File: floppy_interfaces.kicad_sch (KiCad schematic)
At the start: 24 parts, among them J13 Conn_01x04_Male, J14 Conn_02x17_Odd_Even, J16 Conn_01x04_Male, J6 SDF-60J for IEC 1541 serial p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, U1 74LS373, U2 74LVC374, U22 74LS06N, U3 74LVC374, U4 74LS373

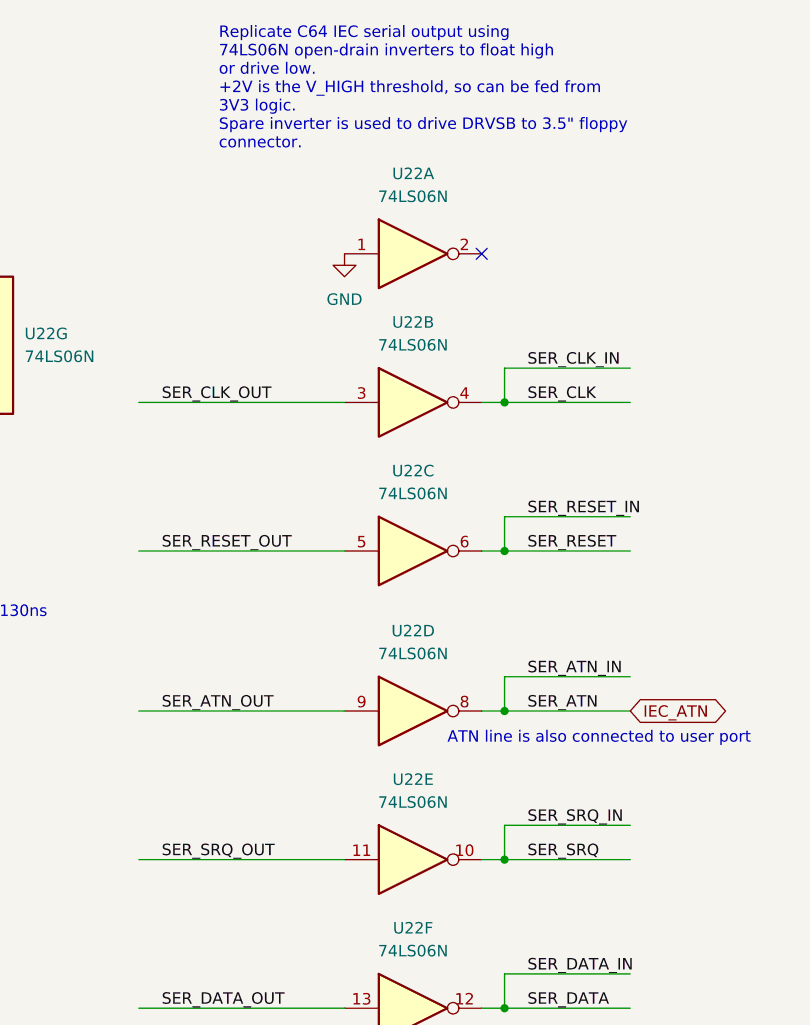
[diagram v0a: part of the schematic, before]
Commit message: route IEC port. Remove duplicate footprints
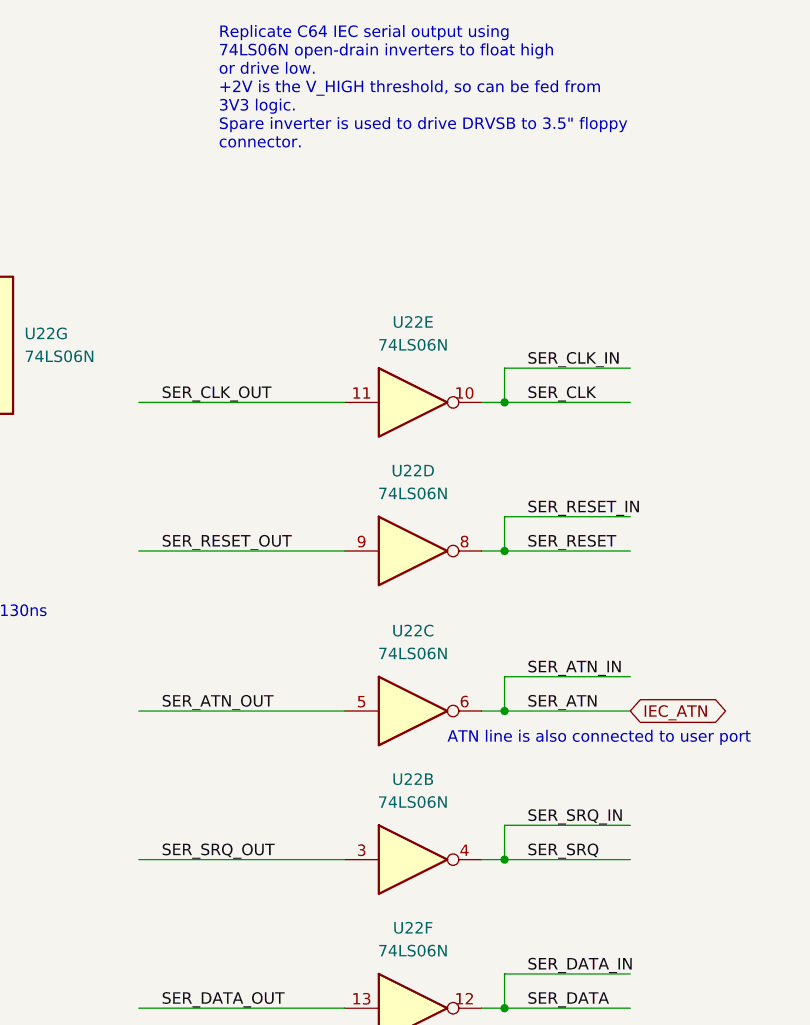
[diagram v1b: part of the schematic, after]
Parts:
- removed unit 1 of U22
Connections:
- net IEC_ATN: now also U22.6; no longer U22.8
- net SER_ATN_OUT: now also U22.5; no longer U22.9
- net SER_CLK: now also U22.10; no longer U22.4
- net SER_CLK_OUT: now also U22.11; no longer U22.3
- net SER_RESET: now also U22.8; no longer U22.6
- net SER_RESET_OUT: now also U22.9; no longer U22.5
- net SER_SRQ: now also U22.4; no longer U22.10
- net SER_SRQ_OUT: now also U22.3; no longer U22.11
- no-connect marks 19 -> 18
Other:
- moved on the sheet: U22B, U22C, U22D, U22E
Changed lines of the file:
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@@
   (no_connect (at 69.85 107.95))
   (no_connect (at 44.45 168.91))
-  (no_connect (at 165.1 45.72))
   (no_connect (at 69.85 168.91))
   (no_connect (at 69.85 171.45))
@@
     (pin "2")
   )
-  (symbol (lib_id "74xx:74LS06N") (at 157.48 45.72 0) (unit 1)
-    (in_bom yes) (on_board yes) (fields_autoplaced)
-    (property "Reference" "U22" (id 0) (at 157.48 36.83 0))
-    (property "Value" "74LS06N" (id 1) (at 157.48 39.37 0))
-    (property "Footprint" "Package_DIP:DIP-14_W7.62mm" (id 2) (at 157.48 45.72 0)
-      (effects (font (size 1.27 1.27)) hide)
-    )
-    (property "Datasheet" "http://www.ti.com/lit/gpn/sn74LS06N" (id 3) (at 157.48 45.72 0)
-      (effects (font (size 1.27 1.27)) hide)
-    )
-    (pin "1")
-    (pin "2")
-  )
   (symbol (lib_id "power:GND") (at 226.06 148.59 0) (unit 1)
     (in_bom yes) (on_board yes) (fields_autoplaced)
@@
     (pin "9")
   )
-  (symbol (lib_id "power:GND") (at 149.86 45.72 0) (unit 1)
-    (in_bom yes) (on_board yes) (fields_autoplaced)
-    (property "Reference" "#PWR0111" (id 0) (at 149.86 52.07 0)
-      (effects (font (size 1.27 1.27)) hide)
-    )
-    (property "Value" "GND" (id 1) (at 149.86 50.8 0))
-    (property "Footprint" "" (id 2) (at 149.86 45.72 0)
-      (effects (font (size 1.27 1.27)) hide)
-    )
-    (property "Datasheet" "" (id 3) (at 149.86 45.72 0)
-      (effects (font (size 1.27 1.27)) hide)
-    )
-    (pin "1")
-  )
   (symbol (lib_id "pspice:R") (at 38.1 97.79 90) (unit 1)
     (in_bom yes) (on_board yes)
@@
     (pin "1")
   )
-  (symbol (lib_id "74xx:74LS06N") (at 157.48 62.23 0) (unit 2)
-    (in_bom yes) (on_board yes) (fields_autoplaced)
-    (property "Reference" "U22" (id 0) (at 157.48 53.34 0))
-    (property "Value" "74LS06N" (id 1) (at 157.48 55.88 0))
-    (property "Footprint" "Package_DIP:DIP-14_W7.62mm" (id 2) (at 157.48 62.23 0)
-      (effects (font (size 1.27 1.27)) hide)
-    )
-    (property "Datasheet" "http://www.ti.com/lit/gpn/sn74LS06N" (id 3) (at 157.48 62.23 0)
+  (symbol (lib_id "74xx:74LS06N") (at 157.48 113.03 0) (unit 2)
+    (in_bom yes) (on_board yes) (fields_autoplaced)
+    (property "Reference" "U22" (id 0) (at 157.48 104.14 0))
+    (property "Value" "74LS06N" (id 1) (at 157.48 106.68 0))
+    (property "Footprint" "Package_DIP:DIP-14_W7.62mm" (id 2) (at 157.48 113.03 0)
+      (effects (font (size 1.27 1.27)) hide)
+    )
+    (property "Datasheet" "http://www.ti.com/lit/gpn/sn74LS06N" (id 3) (at 157.48 113.03 0)
       (effects (font (size 1.27 1.27)) hide)
     )
@@
     (pin "1")
   )
-  (symbol (lib_id "74xx:74LS06N") (at 157.48 78.74 0) (unit 3)
-    (in_bom yes) (on_board yes) (fields_autoplaced)
-    (property "Reference" "U22" (id 0) (at 157.48 69.85 0))
-    (property "Value" "74LS06N" (id 1) (at 157.48 72.39 0))
-    (property "Footprint" "Package_DIP:DIP-14_W7.62mm" (id 2) (at 157.48 78.74 0)
-      (effects (font (size 1.27 1.27)) hide)
-    )
-    (property "Datasheet" "http://www.ti.com/lit/gpn/sn74LS06N" (id 3) (at 157.48 78.74 0)
+  (symbol (lib_id "74xx:74LS06N") (at 157.48 96.52 0) (unit 3)
+    (in_bom yes) (on_board yes) (fields_autoplaced)
+    (property "Reference" "U22" (id 0) (at 157.48 87.63 0))
+    (property "Value" "74LS06N" (id 1) (at 157.48 90.17 0))
+    (property "Footprint" "Package_DIP:DIP-14_W7.62mm" (id 2) (at 157.48 96.52 0)
+      (effects (font (size 1.27 1.27)) hide)
+    )
+    (property "Datasheet" "http://www.ti.com/lit/gpn/sn74LS06N" (id 3) (at 157.48 96.52 0)
       (effects (font (size 1.27 1.27)) hide)
     )
@@
     (pin "6")
   )
-  (symbol (lib_id "74xx:74LS06N") (at 157.48 113.03 0) (unit 5)
-    (in_bom yes) (on_board yes) (fields_autoplaced)
-    (property "Reference" "U22" (id 0) (at 157.48 104.14 0))
-    (property "Value" "74LS06N" (id 1) (at 157.48 106.68 0))
-    (property "Footprint" "Package_DIP:DIP-14_W7.62mm" (id 2) (at 157.48 113.03 0)
-      (effects (font (size 1.27 1.27)) hide)
-    )
-    (property "Datasheet" "http://www.ti.com/lit/gpn/sn74LS06N" (id 3) (at 157.48 113.03 0)
+  (symbol (lib_id "74xx:74LS06N") (at 157.48 62.23 0) (unit 5)
+    (in_bom yes) (on_board yes) (fields_autoplaced)
+    (property "Reference" "U22" (id 0) (at 157.48 53.34 0))
+    (property "Value" "74LS06N" (id 1) (at 157.48 55.88 0))
+    (property "Footprint" "Package_DIP:DIP-14_W7.62mm" (id 2) (at 157.48 62.23 0)
+      (effects (font (size 1.27 1.27)) hide)
+    )
+    (property "Datasheet" "http://www.ti.com/lit/gpn/sn74LS06N" (id 3) (at 157.48 62.23 0)
       (effects (font (size 1.27 1.27)) hide)
     )
@@
     (pin "1")
   )
-  (symbol (lib_id "74xx:74LS06N") (at 157.48 96.52 0) (unit 4)
-    (in_bom yes) (on_board yes) (fields_autoplaced)
-    (property "Reference" "U22" (id 0) (at 157.48 87.63 0))
-    (property "Value" "74LS06N" (id 1) (at 157.48 90.17 0))
-    (property "Footprint" "Package_DIP:DIP-14_W7.62mm" (id 2) (at 157.48 96.52 0)
-      (effects (font (size 1.27 1.27)) hide)
-    )
-    (property "Datasheet" "http://www.ti.com/lit/gpn/sn74LS06N" (id 3) (at 157.48 96.52 0)
-      (effects (font (size 1.27 1.27)) hide)
-    )
+  (symbol (lib_id "74xx:74LS06N") (at 157.48 78.74 0) (unit 4)
+    (in_bom yes) (on_board yes) (fields_autoplaced)
+    (property "Reference" "U22" (id 0) (at 157.48 69.85 0))
+    (property "Value" "74LS06N" (id 1) (at 157.48 72.39 0))
+    (property "Footprint" "Package_DIP:DIP-14_W7.62mm" (id 2) (at 157.48 78.74 0)
+      (effects (font (size 1.27 1.27)) hide)
+    )
+    (property "Datasheet" "http://www.ti.com/lit/gpn/sn74LS06N" (id 3) (at 157.48 78.74 0)
+      (effects (font (size 1.27 1.27)) hide)
+    )

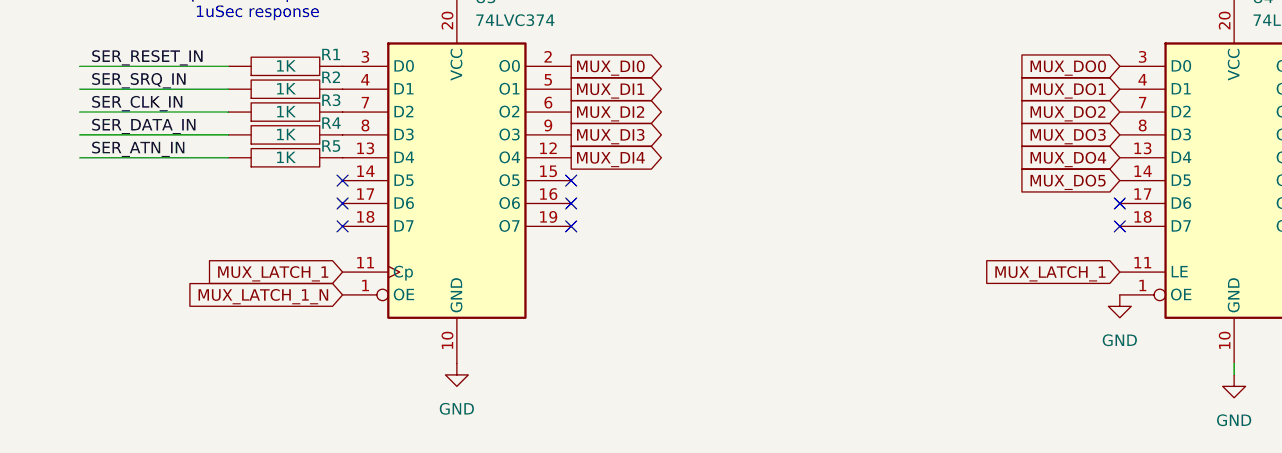
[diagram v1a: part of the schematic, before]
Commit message: renumber MUX registers to ease routing
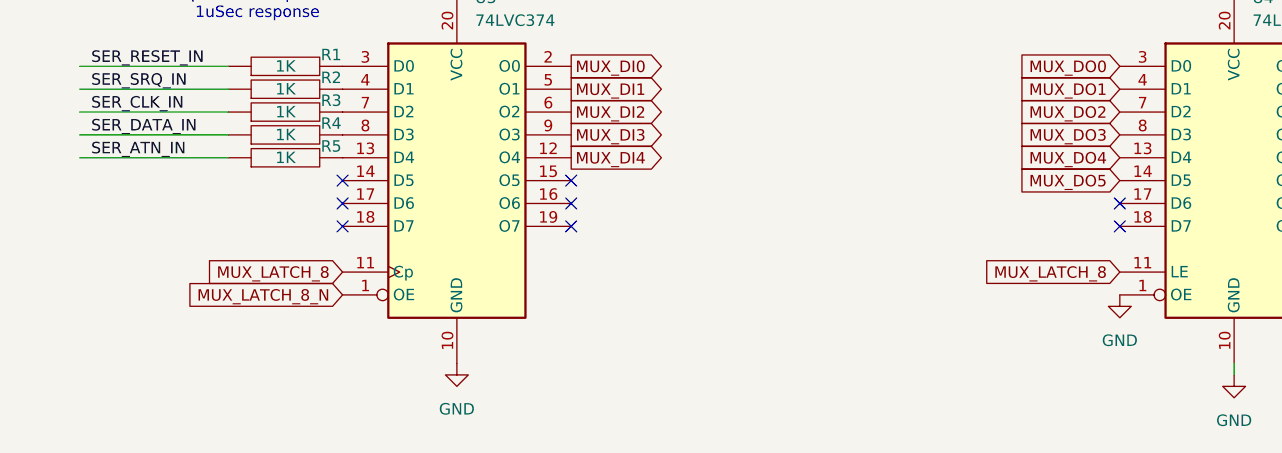
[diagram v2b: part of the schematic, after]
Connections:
- net MUX_LATCH_1 renamed MUX_LATCH_8
- net MUX_LATCH_1_N renamed MUX_LATCH_8_N
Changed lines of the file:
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@@
     )
   )
-  (global_label "MUX_LATCH_1" (shape input) (at 130.81 176.53 180) (fields_autoplaced)
+  (global_label "MUX_LATCH_8" (shape input) (at 130.81 176.53 180) (fields_autoplaced)
     (effects (font (size 1.27 1.27)) (justify right))
     (property "Intersheet References" "${INTERSHEET_REFS}" (id 0) (at 115.5759 176.4506 0)
@@
     )
   )
-  (global_label "MUX_LATCH_1" (shape input) (at 44.45 176.53 180) (fields_autoplaced)
+  (global_label "MUX_LATCH_8" (shape input) (at 44.45 176.53 180) (fields_autoplaced)
     (effects (font (size 1.27 1.27)) (justify right))
     (property "Intersheet References" "${INTERSHEET_REFS}" (id 0) (at 29.2159 176.4506 0)
@@
     )
   )
-  (global_label "MUX_LATCH_1_N" (shape input) (at 44.45 179.07 180) (fields_autoplaced)
+  (global_label "MUX_LATCH_8_N" (shape input) (at 44.45 179.07 180) (fields_autoplaced)
     (effects (font (size 1.27 1.27)) (justify right))
     (property "Intersheet References" "${INTERSHEET_REFS}" (id 0) (at 26.9179 178.9906 0)

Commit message: route u4
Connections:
- net MUX_DO6: now also U4.17 (D6)
- net MUX_DO7: now also U4.18 (D7)
- net SER_DATA_OUT: now also U4.19 (O7); no longer U4.9 (O3)
- no-connect marks 18 -> 16
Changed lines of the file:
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@@
   (no_connect (at 69.85 166.37))
   (no_connect (at 234.95 39.37))
-  (no_connect (at 156.21 171.45))
+  (no_connect (at 156.21 161.29))
   (no_connect (at 69.85 102.87))
-  (no_connect (at 130.81 168.91))
   (no_connect (at 44.45 105.41))
   (no_connect (at 44.45 171.45))
@@
   (no_connect (at 44.45 102.87))
   (no_connect (at 44.45 107.95))
-  (no_connect (at 130.81 171.45))
   (no_connect (at 234.95 41.91))
   (no_connect (at 69.85 107.95))
@@
     (stroke (width 0) (type default) (color 0 0 0 0))
   )
-  (wire (pts (xy 156.21 161.29) (xy 168.91 161.29))
+  (wire (pts (xy 156.21 171.45) (xy 168.91 171.45))
     (stroke (width 0) (type default) (color 0 0 0 0))
   )
@@
     (effects (font (size 1.27 1.27)) (justify left bottom))
   )
-  (label "SER_DATA_OUT" (at 158.75 161.29 0)
+  (label "SER_DATA_OUT" (at 158.75 171.45 0)
     (effects (font (size 1.27 1.27)) (justify left bottom))
   )
@@
     )
   )
+  (global_label "MUX_DO7" (shape input) (at 130.81 171.45 180) (fields_autoplaced)
+    (effects (font (size 1.27 1.27)) (justify right))
+    (property "Intersheet References" "${INTERSHEET_REFS}" (id 0) (at 119.6279 171.3706 0)
+      (effects (font (size 1.27 1.27)) (justify right) hide)
+    )
+  )
   (global_label "MUX_DO0" (shape input) (at 130.81 153.67 180) (fields_autoplaced)
     (effects (font (size 1.27 1.27)) (justify right))
@@
       (effects (font (size 1.27 1.27)) (justify right) hide)
     )
+  )
+  (global_label "MUX_DO6" (shape input) (at 130.81 168.91 180) (fields_autoplaced)
+    (effects (font (size 1.27 1.27)) (justify right))
+    (property "Intersheet References" "${INTERSHEET_REFS}" (id 0) (at 119.6279 168.8306 0)
+      (effects (font (size 1.27 1.27)) (justify right) hide)
+    )
